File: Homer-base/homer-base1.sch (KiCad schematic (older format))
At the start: 18 parts, among them J1 J1 LEFT, J2 J2 DOWN, J3 J3 RIGHT

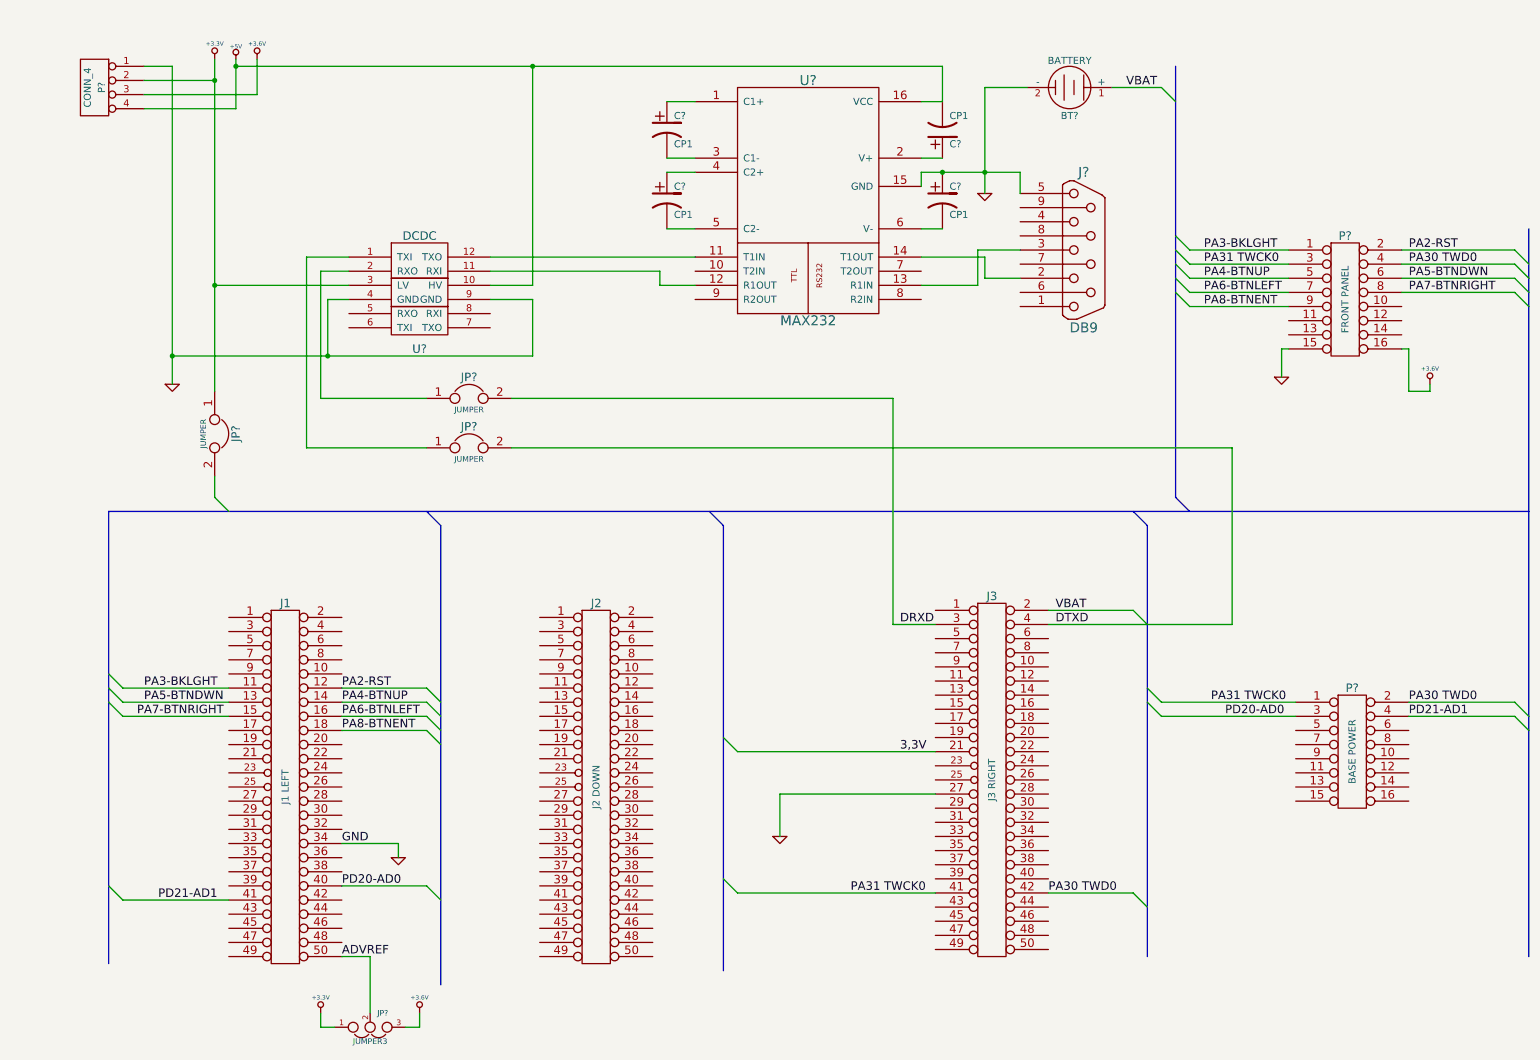
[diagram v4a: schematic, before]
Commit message: Fix Power schematics
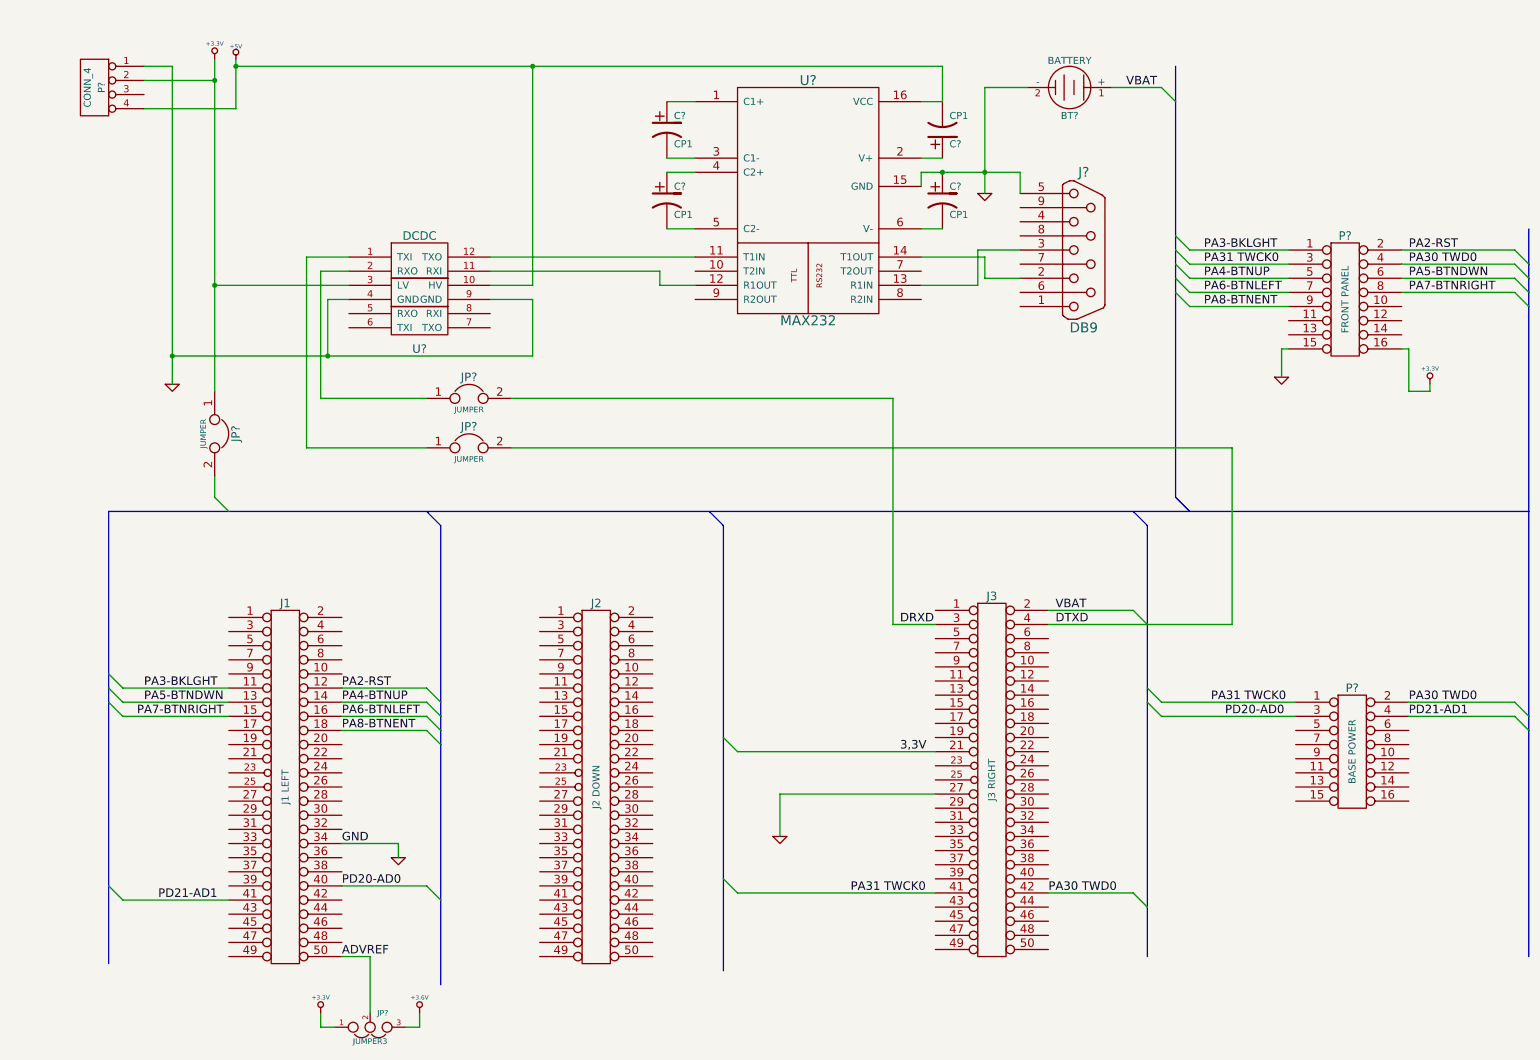
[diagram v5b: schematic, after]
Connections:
- net +3.3V: now also P?.16
- net +3.6V: no longer P?.16, P?.3 (P3)
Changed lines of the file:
@@
 Sheet 1 1
 Title ""
-Date "21 apr 2017"
+Date "10 jun 2017"
 Rev ""
 Comp ""
@@
 	10700 2300 9900 2300
 Wire Bus Line
-	5100 3950 5100 7100
-Wire Bus Line
-	750  3850 750  7050
+	5100 3950 5100 5450
+Wire Bus Line
+	5100 5450 5100 6450
+Wire Bus Line
+	5100 6450 5100 7100
+Wire Bus Line
+	750  3850 750  5000
+Wire Bus Line
+	750  5000 750  5100
+Wire Bus Line
+	750  5100 750  5200
+Wire Bus Line
+	750  5200 750  6500
+Wire Bus Line
+	750  6500 750  7050
 Wire Wire Line
 	1600 5100 850  5100
@@
 	8700 4650 8700 3400
 Wire Wire Line
-	7400 4650 8700 4650
+	7400 4650 8100 4650
+Wire Wire Line
+	8100 4650 8700 4650
 Wire Wire Line
 	5500 6150 5500 5850
@@
 	7200 1450 7200 1600
 Wire Wire Line
-	6500 1450 7200 1450
+	6500 1450 6650 1450
+Wire Wire Line
+	6650 1450 6950 1450
+Wire Wire Line
+	6950 1450 7200 1450
 Wire Wire Line
 	6500 2050 6950 2050
@@
 	6900 2250 6500 2250
 Wire Wire Line
-	6950 850  6950 1600
+	6950 850  6950 1450
+Wire Wire Line
+	6950 1450 6950 1600
 Connection ~ 6950 1450
 Wire Wire Line
@@
 	1600 5200 850  5200
 Wire Bus Line
-	750  3850 10800 3850
-Wire Bus Line
-	10800 1850 10800 7000
-Wire Bus Line
-	8100 3950 8100 7000
+	750  3850 1600 3850
+Wire Bus Line
+	1600 3850 3000 3850
+Wire Bus Line
+	3000 3850 5000 3850
+Wire Bus Line
+	5000 3850 8000 3850
+Wire Bus Line
+	8000 3850 8400 3850
+Wire Bus Line
+	8400 3850 10800 3850
+Wire Bus Line
+	10800 1850 10800 2100
+Wire Bus Line
+	10800 2100 10800 2200
+Wire Bus Line
+	10800 2200 10800 2300
+Wire Bus Line
+	10800 2300 10800 2400
+Wire Bus Line
+	10800 2400 10800 5300
+Wire Bus Line
+	10800 5300 10800 5400
+Wire Bus Line
+	10800 5400 10800 7000
+Wire Bus Line
+	8100 3950 8100 4650
+Wire Bus Line
+	8100 4650 8100 5100
+Wire Bus Line
+	8100 5100 8100 5200
+Wire Bus Line
+	8100 5200 8100 6650
+Wire Bus Line
+	8100 6650 8100 7000
 Wire Wire Line
 	8000 6550 7400 6550
@@
 	6600 6550 5200 6550
 Wire Bus Line
-	3100 3950 3100 7200
+	3100 3950 3100 5200
+Wire Bus Line
+	3100 5200 3100 5300
+Wire Bus Line
+	3100 5300 3100 5400
+Wire Bus Line
+	3100 5400 3100 5500
+Wire Bus Line
+	3100 5500 3100 6600
+Wire Bus Line
+	3100 6600 3100 7200
 Wire Wire Line
 	3000 5200 2400 5200
@@
 	2400 5300 3000 5300
 Wire Bus Line
-	8300 700  8300 3750
+	8300 700  8300 950
+Wire Bus Line
+	8300 950  8300 1900
+Wire Bus Line
+	8300 1900 8300 2000
+Wire Bus Line
+	8300 2000 8300 2100
+Wire Bus Line
+	8300 2100 8300 2200
+Wire Bus Line
+	8300 2200 8300 2300
+Wire Bus Line
+	8300 2300 8300 3750
 Entry Wire Line
 	3000 5400 3100 5500
@@
 $EndComp
 Wire Wire Line
-	1200 700  1200 2950
+	1200 700  1200 2750
+Wire Wire Line
+	1200 2750 1200 2950
 $Comp
 L +3.3V #PWR?
@@
 $EndComp
 Wire Wire Line
-	1500 650  1500 3000
+	1500 650  1500 800
+Wire Wire Line
+	1500 800  1500 2250
+Wire Wire Line
+	1500 2250 1500 3000
 Entry Wire Line
 	1500 3750 1600 3850
@@
 	3750 2350 3750 2750
 Wire Wire Line
-	3750 2750 1200 2750
+	3750 2750 2300 2750
+Wire Wire Line
+	2300 2750 1200 2750
 Wire Wire Line
 	2450 2350 2300 2350
@@
 	2300 2350 2300 2750
 Connection ~ 2300 2750
-$Comp
-L +3.6V #PWR?
-U 1 1 56867349
-P 10100 2950
-F 0 "#PWR?" H 10100 2910 30  0001 C CNN
-F 1 "+3.6V" H 10100 3060 30  0000 C CNN
-F 2 "" H 10100 2950 60  0000 C CNN
-F 3 "" H 10100 2950 60  0000 C CNN
-	1    10100 2950
-	1    0    0    -1
-$EndComp
-Wire Wire Line
-	1650 650  1650 1000
-$Comp
-L +3.6V #PWR?
-U 1 1 56867700
-P 1800 650
-F 0 "#PWR?" H 1800 610 30  0001 C CNN
-F 1 "+3.6V" H 1800 760 30  0000 C CNN
-F 2 "" H 1800 650 60  0000 C CNN
-F 3 "" H 1800 650 60  0000 C CNN
-	1    1800 650
-	1    0    0    -1
-$EndComp
+Wire Wire Line
+	1650 650  1650 700
+Wire Wire Line
+	1650 700  1650 1000
 Entry Wire Line
 	8300 1900 8400 2000
@@
 Connection ~ 3750 700
 Wire Wire Line
-	1800 650  1800 900
-Wire Wire Line
-	1650 700  6650 700
+	1650 700  3750 700
+Wire Wire Line
+	3750 700  6650 700
 Connection ~ 1200 2750
 Wire Wire Line
@@
 	1650 1000 1000 1000
 Connection ~ 1650 700
-Wire Wire Line
-	1800 900  1000 900
 Wire Wire Line
 	1000 800  1500 800
@@
 Wire Wire Line
 	2250 7500 2250 7400
+$Comp
+L +3,3V #PWR?
+U 1 1 593C29D9
+P 10100 2950
+F 0 "#PWR?" H 10100 2910 30  0001 C CNN
+F 1 "+3,3V" H 10100 3060 30  0000 C CNN
+F 2 "" H 10100 2950 60  0000 C CNN
+F 3 "" H 10100 2950 60  0000 C CNN
+	1    10100 2950
+	1    0    0    -1
+$EndComp
 $EndSCHEMATC

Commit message: fix adc vref
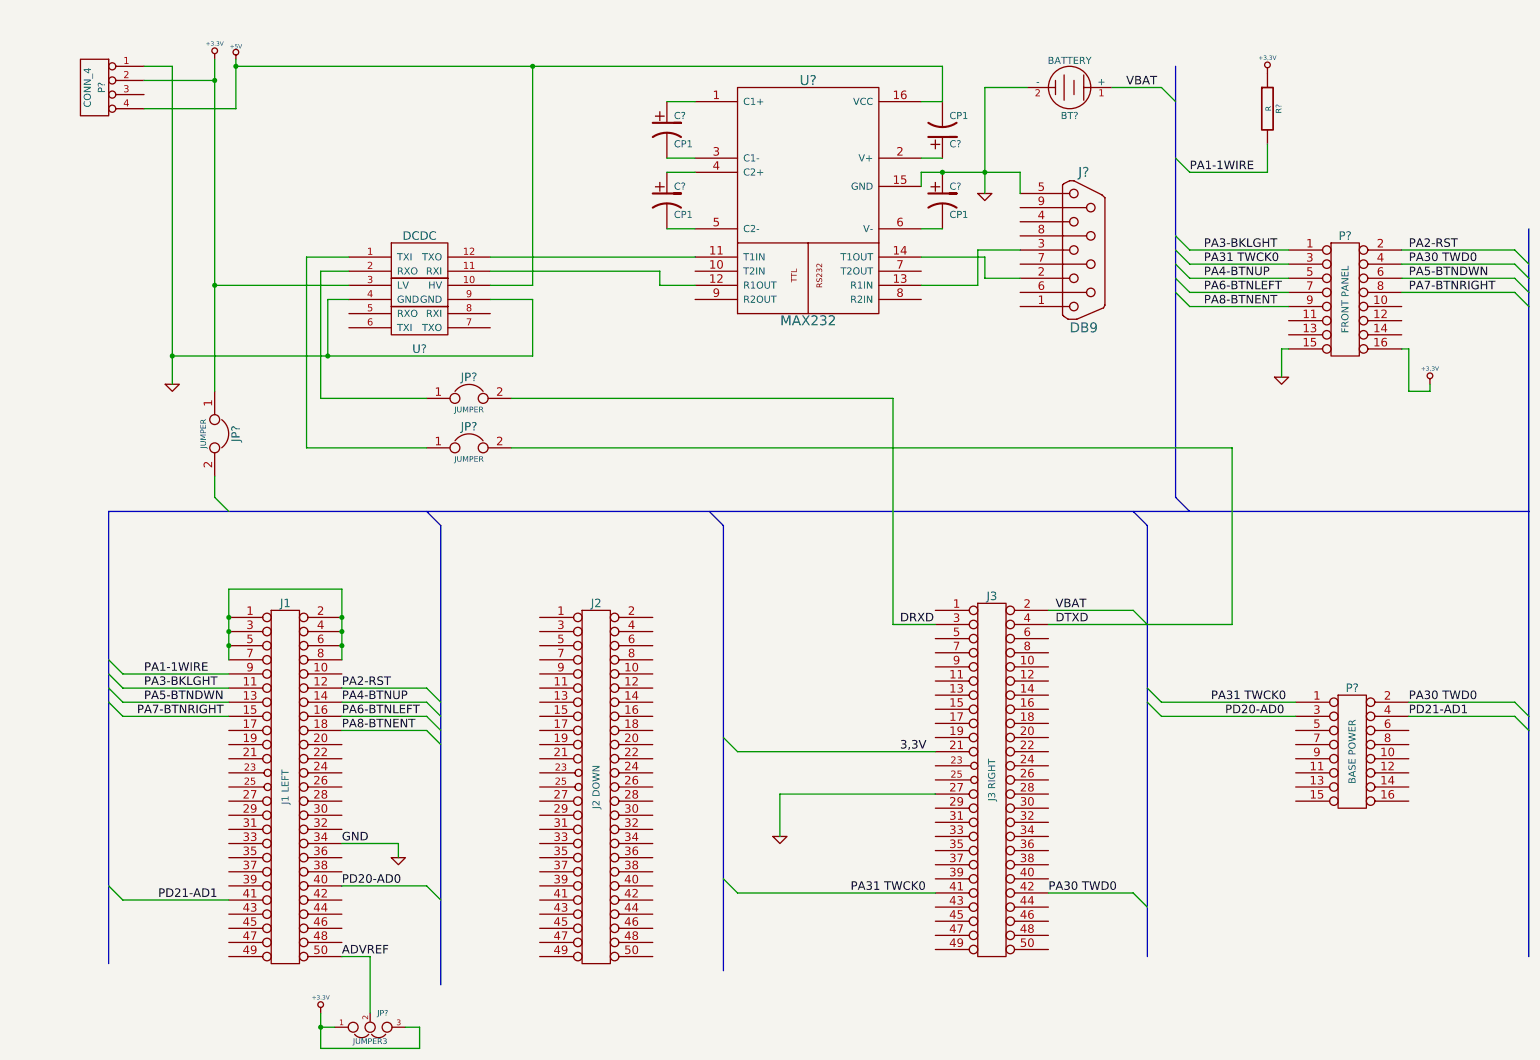
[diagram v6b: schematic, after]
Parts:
- added R?: R, ~, symbol R
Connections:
- net +3.6V is gone; now on net +3.3V: JP?.3
- net +3.3V: now also R?.1
- net at J1.1 (P1): now also J1.2 (P2), J1.3 (P3), J1.4 (P4), J1.5 (P5), J1.6 (P6), J1.7 (P7), J1.8 (P8)
- net PA1-1WIRE: now reaches J1.9 (P9)
- net PA1-1WIRE: now also R?.2
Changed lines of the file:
@@
 Sheet 1 1
 Title ""
-Date "10 jun 2017"
+Date "16 jun 2017"
 Rev ""
 Comp ""
@@
 	10700 2300 9900 2300
 Wire Bus Line
-	5100 3950 5100 5450
+	5100 3950 5100 7100
 Wire Bus Line
-	5100 5450 5100 6450
-Wire Bus Line
-	5100 6450 5100 7100
-Wire Bus Line
-	750  3850 750  5000
-Wire Bus Line
-	750  5000 750  5100
-Wire Bus Line
-	750  5100 750  5200
-Wire Bus Line
-	750  5200 750  6500
-Wire Bus Line
-	750  6500 750  7050
+	750  3850 750  7050
 Wire Wire Line
 	1600 5100 850  5100
@@
 	8700 4650 8700 3400
 Wire Wire Line
-	7400 4650 8100 4650
-Wire Wire Line
-	8100 4650 8700 4650
+	7400 4650 8700 4650
 Wire Wire Line
 	5500 6150 5500 5850
@@
 	7200 1450 7200 1600
 Wire Wire Line
-	6500 1450 6650 1450
-Wire Wire Line
-	6650 1450 6950 1450
-Wire Wire Line
-	6950 1450 7200 1450
+	6500 1450 7200 1450
 Wire Wire Line
 	6500 2050 6950 2050
@@
 	6900 2250 6500 2250
 Wire Wire Line
-	6950 850  6950 1450
-Wire Wire Line
-	6950 1450 6950 1600
+	6950 850  6950 1600
 Connection ~ 6950 1450
 Wire Wire Line
@@
 	1600 5200 850  5200
 Wire Bus Line
-	750  3850 1600 3850
+	750  3850 10800 3850
 Wire Bus Line
-	1600 3850 3000 3850
+	10800 1850 10800 7000
 Wire Bus Line
-	3000 3850 5000 3850
-Wire Bus Line
-	5000 3850 8000 3850
-Wire Bus Line
-	8000 3850 8400 3850
-Wire Bus Line
-	8400 3850 10800 3850
-Wire Bus Line
-	10800 1850 10800 2100
-Wire Bus Line
-	10800 2100 10800 2200
-Wire Bus Line
-	10800 2200 10800 2300
-Wire Bus Line
-	10800 2300 10800 2400
-Wire Bus Line
-	10800 2400 10800 5300
-Wire Bus Line
-	10800 5300 10800 5400
-Wire Bus Line
-	10800 5400 10800 7000
-Wire Bus Line
-	8100 3950 8100 4650
-Wire Bus Line
-	8100 4650 8100 5100
-Wire Bus Line
-	8100 5100 8100 5200
-Wire Bus Line
-	8100 5200 8100 6650
-Wire Bus Line
-	8100 6650 8100 7000
+	8100 3950 8100 7000
 Wire Wire Line
 	8000 6550 7400 6550
@@
 	6600 6550 5200 6550
 Wire Bus Line
-	3100 3950 3100 5200
-Wire Bus Line
-	3100 5200 3100 5300
-Wire Bus Line
-	3100 5300 3100 5400
-Wire Bus Line
-	3100 5400 3100 5500
-Wire Bus Line
-	3100 5500 3100 6600
-Wire Bus Line
-	3100 6600 3100 7200
+	3100 3950 3100 7200
 Wire Wire Line
 	3000 5200 2400 5200
@@
 	2400 5300 3000 5300
 Wire Bus Line
-	8300 700  8300 950
-Wire Bus Line
-	8300 950  8300 1900
-Wire Bus Line
-	8300 1900 8300 2000
-Wire Bus Line
-	8300 2000 8300 2100
-Wire Bus Line
-	8300 2100 8300 2200
-Wire Bus Line
-	8300 2200 8300 2300
-Wire Bus Line
-	8300 2300 8300 3750
+	8300 700  8300 3750
 Entry Wire Line
 	3000 5400 3100 5500
@@
 $EndComp
 Wire Wire Line
-	1200 700  1200 2750
-Wire Wire Line
-	1200 2750 1200 2950
+	1200 700  1200 2950
 $Comp
 L +3.3V #PWR?
@@
 $EndComp
 Wire Wire Line
-	1500 650  1500 800
-Wire Wire Line
-	1500 800  1500 2250
-Wire Wire Line
-	1500 2250 1500 3000
+	1500 650  1500 3000
 Entry Wire Line
 	1500 3750 1600 3850
@@
 	3750 2350 3750 2750
 Wire Wire Line
-	3750 2750 2300 2750
-Wire Wire Line
-	2300 2750 1200 2750
+	3750 2750 1200 2750
 Wire Wire Line
 	2450 2350 2300 2350
@@
 Connection ~ 2300 2750
 Wire Wire Line
-	1650 650  1650 700
-Wire Wire Line
-	1650 700  1650 1000
+	1650 650  1650 1000
 Entry Wire Line
 	8300 1900 8400 2000
@@
 Connection ~ 3750 700
 Wire Wire Line
-	1650 700  3750 700
-Wire Wire Line
-	3750 700  6650 700
+	1650 700  6650 700
 Connection ~ 1200 2750
 Wire Wire Line
@@
 $EndComp
 $Comp
-L +3.6V #PWR?
-U 1 1 58F9A75B
-P 2950 7400
-F 0 "#PWR?" H 2950 7360 30  0001 C CNN
-F 1 "+3.6V" H 2950 7510 30  0000 C CNN
-F 2 "" H 2950 7400 60  0000 C CNN
-F 3 "" H 2950 7400 60  0000 C CNN
-	1    2950 7400
-	1    0    0    -1
-$EndComp
-$Comp
 L JUMPER3 JP?
 U 1 1 58F9A76A
@@
 	2600 7000 2600 7400
 Wire Wire Line
-	2850 7500 2950 7500
-Wire Wire Line
-	2950 7500 2950 7400
-Wire Wire Line
 	2350 7500 2250 7500
 Wire Wire Line
-	2250 7500 2250 7400
+	2250 7400 2250 7650
 $Comp
 L +3,3V #PWR?
@@
 	1    0    0    -1
 $EndComp
+Wire Wire Line
+	1600 4400 1600 4900
+Connection ~ 1600 4600
+Connection ~ 1600 4700
+Connection ~ 1600 4800
+Wire Wire Line
+	1600 4400 2400 4400
+Wire Wire Line
+	2400 4400 2400 4900
+Connection ~ 2400 4600
+Connection ~ 2400 4700
+Connection ~ 2400 4800
+Wire Wire Line
+	1600 5000 850  5000
+Entry Wire Line
+	750  4900 850  5000
+Text Label 1000 5000 0    60   ~ 0
+PA1-1WIRE
+$Comp
+L +3,3V #PWR?
+U 1 1 5943FF3F
+P 8950 750
+F 0 "#PWR?" H 8950 710 30  0001 C CNN
+F 1 "+3,3V" H 8950 860 30  0000 C CNN
+F 2 "" H 8950 750 60  0000 C CNN
+F 3 "" H 8950 750 60  0000 C CNN
+	1    8950 750
+	1    0    0    -1
+$EndComp
+$Comp
+L R R?
+U 1 1 5943FF4E
+P 8950 1000
+F 0 "R?" V 9030 1000 40  0000 C CNN
+F 1 "R" V 8957 1001 40  0000 C CNN
+F 2 "~" V 8880 1000 30  0000 C CNN
+F 3 "~" H 8950 1000 30  0000 C CNN
+	1    8950 1000
+	1    0    0    -1
+$EndComp
+Entry Wire Line
+	8300 1350 8400 1450
+Wire Wire Line
+	8400 1450 8950 1450
+Wire Wire Line
+	8950 1450 8950 1250
+Text Label 8400 1450 0    60   ~ 0
+PA1-1WIRE
+Wire Wire Line
+	2850 7500 2950 7500
+Wire Wire Line
+	2950 7500 2950 7650
+Wire Wire Line
+	2950 7650 2250 7650
+Connection ~ 2250 7500
 $EndSCHEMATC
